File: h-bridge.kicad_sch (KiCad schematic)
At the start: 17 parts, among them M3 DC, Q3 Q_NMOS, Q4 Q_NMOS, Q5 Q_NMOS, Q6 Q_NMOS, U6 DRV8701

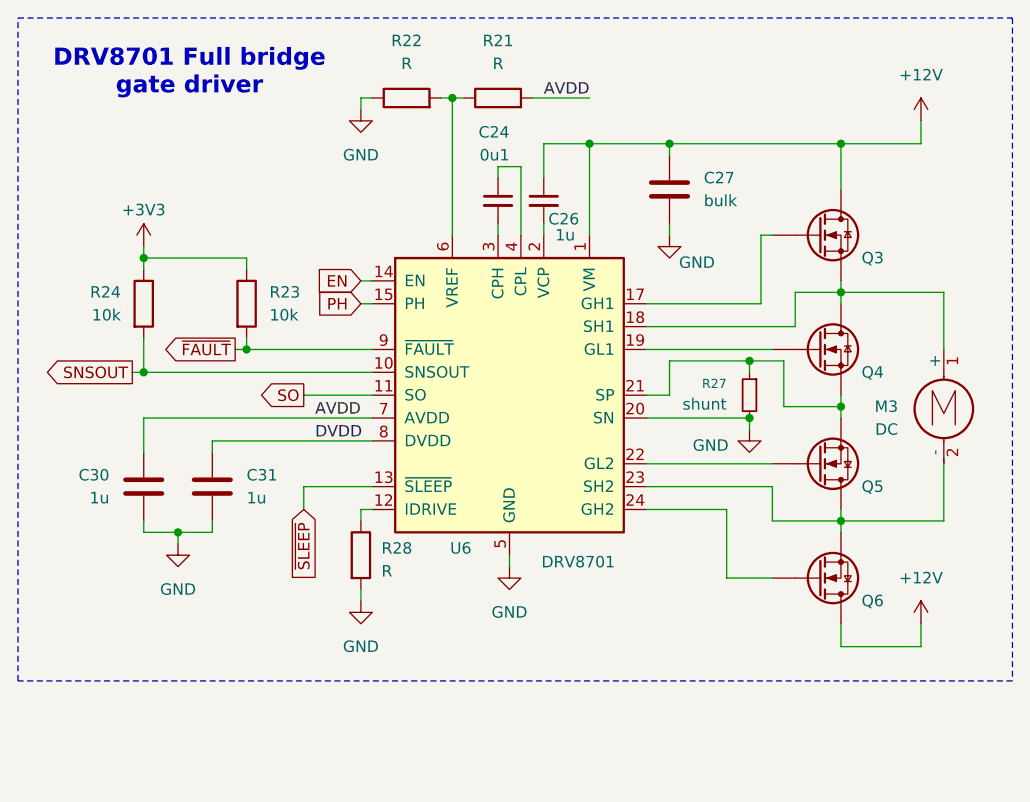
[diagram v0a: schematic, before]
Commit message: schem: add DRV8701 component values
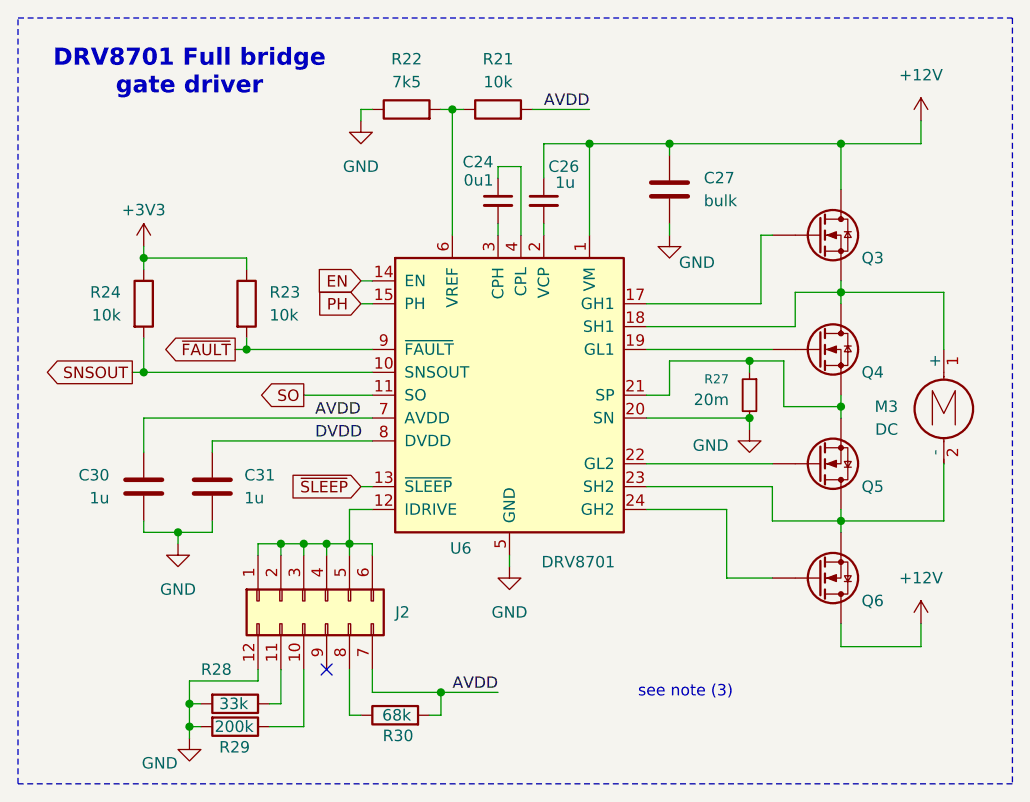
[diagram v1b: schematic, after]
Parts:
- added J2: Conn_02x06_Counter_Clockwise, symbol Connector_Generic:Conn_02x06_Counter_Clockwise
- added R29: 200k, symbol Device:R
- added R30: 68k, symbol Device:R
- R21: value R -> 10k
- R22: value R -> 7k5
- R27: value shunt -> 20m
- R28: value R -> 33k
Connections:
- net AVDD: now also J2.7 (Pin_7), R30.2
- net GND: now also J2.12 (Pin_12), R29.2
- net at U6.12 (IDRIVE): now also J2.1 (Pin_1), J2.2 (Pin_2), J2.3 (Pin_3), J2.4 (Pin_4), J2.5 (Pin_5), J2.6 (Pin_6); no longer R28.1
- new net: J2.10 (Pin_10), R29.1
- new net: J2.8 (Pin_8), R30.1
- new net: J2.11 (Pin_11), R28.1
- no-connect marks 0 -> 1
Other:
- note added: "see note (3)"
- moved on the sheet: R21, R22

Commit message: schem: add Vin driver input selection circuit
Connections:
- net +12V renamed +Vdc
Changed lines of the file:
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@@
-	)
-	(symbol
-		(lib_id "power:+12V")
-		(at 193.04 111.76 0)
-		(unit 1)
-		(exclude_from_sim no)
-		(in_bom yes)
-		(on_board yes)
-		(dnp no)
-		(fields_autoplaced yes)
-		(property "Reference" "#PWR064"
-			(at 193.04 115.57 0)
-			(effects
-				(font
-					(size 1.27 1.27)
-				)
-				(hide yes)
-			)
-		)
-		(property "Value" "+12V"
-			(at 193.04 106.68 0)
-			(effects
-				(font
-					(size 1.27 1.27)
-				)
-			)
-		)
-		(property "Footprint" ""
-			(at 193.04 111.76 0)
-			(effects
-				(font
-					(size 1.27 1.27)
-				)
-				(hide yes)
-			)
-		)
-		(property "Datasheet" ""
-			(at 193.04 111.76 0)
-			(effects
-				(font
-					(size 1.27 1.27)
-				)
-				(hide yes)
-			)
-		)
-		(property "Description" "Power symbol creates a global label with name \"+12V\""
-			(at 193.04 111.76 0)
-			(effects
-				(font
-					(size 1.27 1.27)
-				)
-				(hide yes)
-			)
-		)
-		(pin "1"
-		)
-		(instances
-			(project "motor-power-poc"
-				(path "/a1dc4c9e-7b20-4b66-a693-9133bc644c6b/234f18ec-899d-4a38-bb51-5ceaab0ae171"
-					(reference "#PWR064")
-					(unit 1)
-				)
-			)
-		)
 	)
 	(symbol
@@
 	)
 	(symbol
-		(lib_id "power:+12V")
-		(at 193.04 55.88 0)
-		(unit 1)
-		(exclude_from_sim no)
-		(in_bom yes)
-		(on_board yes)
-		(dnp no)
-		(fields_autoplaced yes)
-		(property "Reference" "#PWR059"
-			(at 193.04 59.69 0)
-			(effects
-				(font
-					(size 1.27 1.27)
-				)
-				(hide yes)
-			)
-		)
-		(property "Value" "+12V"
-			(at 193.04 50.8 0)
-			(effects
-				(font
-					(size 1.27 1.27)
-				)
-			)
-		)
-		(property "Footprint" ""
-			(at 193.04 55.88 0)
-			(effects
-				(font
-					(size 1.27 1.27)
-				)
-				(hide yes)
-			)
-		)
-		(property "Datasheet" ""
-			(at 193.04 55.88 0)
-			(effects
-				(font
-					(size 1.27 1.27)
-				)
-				(hide yes)
-			)
-		)
-		(property "Description" "Power symbol creates a global label with name \"+12V\""
-			(at 193.04 55.88 0)
-			(effects
-				(font
-					(size 1.27 1.27)
-				)
-				(hide yes)
-			)
-		)
-		(pin "1"
-		)
-		(instances
-			(project ""
-				(path "/a1dc4c9e-7b20-4b66-a693-9133bc644c6b/234f18ec-899d-4a38-bb51-5ceaab0ae171"
-					(reference "#PWR059")
-					(unit 1)
-				)
-			)
-		)
-	)
-	(symbol
 		(lib_id "Device:R")
 		(at 135.89 54.61 90)
@@
 				(path "/a1dc4c9e-7b20-4b66-a693-9133bc644c6b/234f18ec-899d-4a38-bb51-5ceaab0ae171"
 					(reference "R22")
+					(unit 1)
+				)
+			)
+		)
+	)
+	(symbol
+		(lib_id "power:+12V")
+		(at 193.04 111.76 0)
+		(unit 1)
+		(exclude_from_sim no)
+		(in_bom yes)
+		(on_board yes)
+		(dnp no)
+		(property "Reference" "#PWR064"
+			(at 193.04 115.57 0)
+			(effects
+				(font
+					(size 1.27 1.27)
+				)
+				(hide yes)
+			)
+		)
+		(property "Value" "+Vdc"
+			(at 193.04 107.442 0)
+			(effects
+				(font
+					(size 1.27 1.27)
+				)
+			)
+		)
+		(property "Footprint" ""
+			(at 193.04 111.76 0)
+			(effects
+				(font
+					(size 1.27 1.27)
+				)
+				(hide yes)
+			)
+		)
+		(property "Datasheet" ""
+			(at 193.04 111.76 0)
+			(effects
+				(font
+					(size 1.27 1.27)
+				)
+				(hide yes)
+			)
+		)
+		(property "Description" "Power symbol creates a global label with name \"+12V\""
+			(at 193.04 111.76 0)
+			(effects
+				(font
+					(size 1.27 1.27)
+				)
+				(hide yes)
+			)
+		)
+		(pin "1"
+		)
+		(instances
+			(project "motor-power-poc"
+				(path "/a1dc4c9e-7b20-4b66-a693-9133bc644c6b/234f18ec-899d-4a38-bb51-5ceaab0ae171"
+					(reference "#PWR064")
 					(unit 1)
 				)
@@
 					(unit 1)
 				)
+			)
+		)
+	)
+	(symbol
+		(lib_id "power:+12V")
+		(at 193.04 55.88 0)
+		(unit 1)
+		(exclude_from_sim no)
+		(in_bom yes)
+		(on_board yes)
+		(dnp no)
+		(property "Reference" "#PWR078"
+			(at 193.04 59.69 0)
+			(effects
+				(font
+					(size 1.27 1.27)
+				)
+				(hide yes)
+			)
+		)
+		(property "Value" "+Vdc"
+			(at 193.04 51.562 0)
+			(effects
+				(font
+					(size 1.27 1.27)
+				)
+			)
+		)
+		(property "Footprint" ""
+			(at 193.04 55.88 0)
+			(effects
+				(font
+					(size 1.27 1.27)
+				)
+				(hide yes)
+			)
+		)
+		(property "Datasheet" ""
+			(at 193.04 55.88 0)
+			(effects
+				(font
+					(size 1.27 1.27)
+				)
+				(hide yes)
+			)
+		)
+		(property "Description" "Power symbol creates a global label with name \"+12V\""
+			(at 193.04 55.88 0)
+			(effects
+				(font
+					(size 1.27 1.27)
+				)
+				(hide yes)
+			)
+		)
+		(pin "1"
+		)
+		(instances
+			(project "motor-power-poc"
+				(path "/a1dc4c9e-7b20-4b66-a693-9133bc644c6b/234f18ec-899d-4a38-bb51-5ceaab0ae171"
+					(reference "#PWR078")
+					(unit 1)
+				)

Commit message: schem: add pins to hierachical sheets
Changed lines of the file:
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@@
 	(wire
 		(pts
-			(xy 193.04 114.3) (xy 184.15 114.3)
+			(xy 191.77 114.3) (xy 184.15 114.3)
 		)
 		(stroke
@@
 	(wire
 		(pts
-			(xy 184.15 58.42) (xy 193.04 58.42)
+			(xy 184.15 58.42) (xy 191.77 58.42)
 		)
 		(stroke
@@
 		(pts
 			(xy 138.43 121.92) (xy 139.7 121.92)
-		)
-		(stroke
-			(width 0)
-			(type default)
-		)
-	)
-	(wire
-		(pts
-			(xy 193.04 111.76) (xy 193.04 114.3)
-		)
-		(stroke
-			(width 0)
-			(type default)
-		)
-	)
-	(wire
-		(pts
-			(xy 193.04 55.88) (xy 193.04 58.42)
 		)
 		(stroke
@@
 				(hide yes)
 			)
+		)
+	)
+	(hierarchical_label "+Vdc"
+		(shape input)
+		(at 191.77 58.42 0)
+		(effects
+			(font
+				(size 1.27 1.27)
+			)
+			(justify left)
+		)
+	)
+	(hierarchical_label "+Vdc"
+		(shape input)
+		(at 191.77 114.3 0)
+		(effects
+			(font
+				(size 1.27 1.27)
+			)
+			(justify left)
 		)
 	)
@@
 				(path "/a1dc4c9e-7b20-4b66-a693-9133bc644c6b/234f18ec-899d-4a38-bb51-5ceaab0ae171"
 					(reference "R22")
-					(unit 1)
-				)
-			)
-		)
-	)
-	(symbol
-		(lib_id "power:+12V")
-		(at 193.04 111.76 0)
-		(unit 1)
-		(exclude_from_sim no)
-		(in_bom yes)
-		(on_board yes)
-		(dnp no)
-		(property "Reference" "#PWR064"
-			(at 193.04 115.57 0)
-			(effects
-				(font
-					(size 1.27 1.27)
-				)
-				(hide yes)
-			)
-		)
-		(property "Value" "+Vdc"
-			(at 193.04 107.442 0)
-			(effects
-				(font
-					(size 1.27 1.27)
-				)
-			)
-		)
-		(property "Footprint" ""
-			(at 193.04 111.76 0)
-			(effects
-				(font
-					(size 1.27 1.27)
-				)
-				(hide yes)
-			)
-		)
-		(property "Datasheet" ""
-			(at 193.04 111.76 0)
-			(effects
-				(font
-					(size 1.27 1.27)
-				)
-				(hide yes)
-			)
-		)
-		(property "Description" "Power symbol creates a global label with name \"+12V\""
-			(at 193.04 111.76 0)
-			(effects
-				(font
-					(size 1.27 1.27)
-				)
-				(hide yes)
-			)
-		)
-		(pin "1"
-		)
-		(instances
-			(project "motor-power-poc"
-				(path "/a1dc4c9e-7b20-4b66-a693-9133bc644c6b/234f18ec-899d-4a38-bb51-5ceaab0ae171"
-					(reference "#PWR064")
 					(unit 1)
 				)
@@
 					(unit 1)
 				)
-			)
-		)
-	)
-	(symbol
-		(lib_id "power:+12V")
-		(at 193.04 55.88 0)
-		(unit 1)
-		(exclude_from_sim no)
-		(in_bom yes)
-		(on_board yes)
-		(dnp no)
-		(property "Reference" "#PWR078"
-			(at 193.04 59.69 0)
-			(effects
-				(font
-					(size 1.27 1.27)
-				)
-				(hide yes)
-			)
-		)
-		(property "Value" "+Vdc"
-			(at 193.04 51.562 0)
-			(effects
-				(font
-					(size 1.27 1.27)
-				)
-			)
-		)
-		(property "Footprint" ""
-			(at 193.04 55.88 0)
-			(effects
-				(font
-					(size 1.27 1.27)
-				)
-				(hide yes)
-			)
-		)
-		(property "Datasheet" ""
-			(at 193.04 55.88 0)
-			(effects
-				(font
-					(size 1.27 1.27)
-				)
-				(hide yes)
-			)
-		)
-		(property "Description" "Power symbol creates a global label with name \"+12V\""
-			(at 193.04 55.88 0)
-			(effects
-				(font
-					(size 1.27 1.27)
-				)
-				(hide yes)
-			)
-		)
-		(pin "1"
-		)
-		(instances
-			(project "motor-power-poc"
-				(path "/a1dc4c9e-7b20-4b66-a693-9133bc644c6b/234f18ec-899d-4a38-bb51-5ceaab0ae171"
-					(reference "#PWR078")
-					(unit 1)
-				)
